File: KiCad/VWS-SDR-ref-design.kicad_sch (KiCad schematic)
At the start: 99 parts, among them J1 RF_IN, J10 IF breakout, J2 IQ_Out, J3 SI5351 board, J4 Conn_01x20_Socket, J5 Conn_01x20_Socket, J6 I2C breakout, J7 Power breakout, J8 GPIO Breakout, J9 GPIO Breakout, U1 GALI-S66, U2 74CBTLV3253DR, U3 MC33078, U4 MC33078, U5 RASPBERRY-PICO

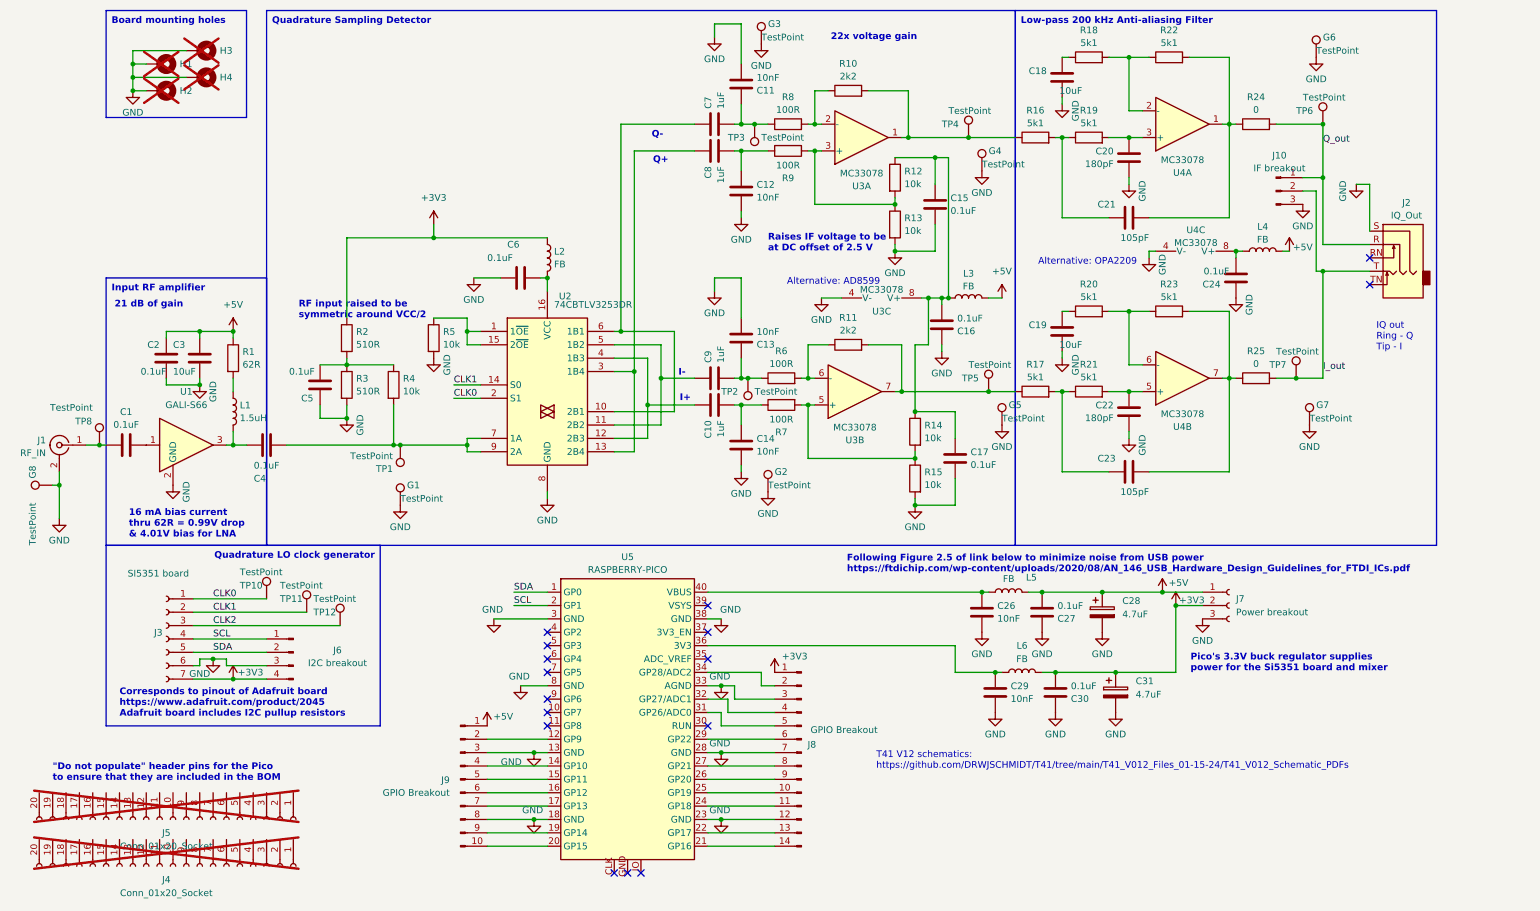
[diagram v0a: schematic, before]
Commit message: Cleaned up the schematic (removed unnecessary components), replaced R/C footprints with 0603, replaced testpoints wit smd footprints, made mounting holes smaller
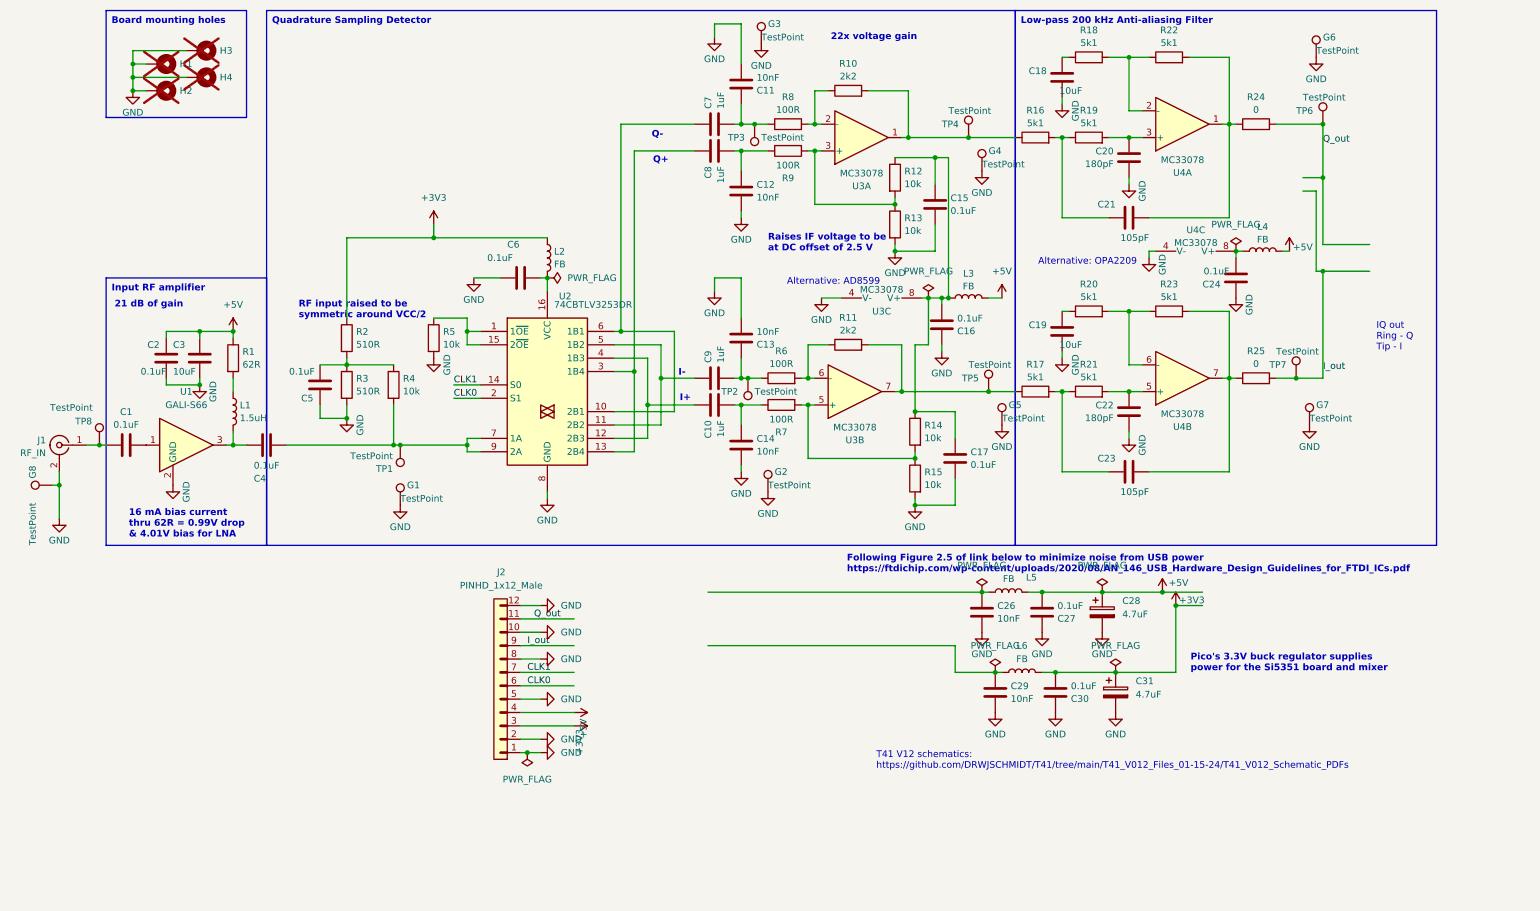
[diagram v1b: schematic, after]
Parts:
- removed J10: IF breakout, symbol Connector:Conn_01x03_Pin
- removed J2: IQ_Out, VWS-SDR:Jack_3.5mm_STX-3081_Horizontal, symbol Connector_Audio:AudioJack3_SwitchTR
- removed J3: SI5351 board, VWS-SDR:Adafruit_Si5351, symbol Connector:Conn_01x07_Socket
- removed J4, J5: Conn_01x20_Socket, symbol Connector:Conn_01x20_Socket
- removed J6: I2C breakout, Connector_PinHeader_2.54mm:PinHeader_1x04_P2.54mm_Vertical, symbol Connector:Conn_01x04_Pin
- removed J7: Power breakout, Connector_PinHeader_2.54mm:PinHeader_1x03_P2.54mm_Vertical, symbol Connector:Conn_01x03_Socket
- removed J8: GPIO Breakout, symbol Connector:Conn_01x14_Pin
- removed J9: GPIO Breakout, symbol Connector:Conn_01x10_Pin
- removed TP10, TP11, TP12: TestPoint, Connector_PinHeader_2.54mm:PinHeader_1x01_P2.54mm_Vertical, symbol Connector:TestPoint
- removed U5: RASPBERRY-PICO, VWS-SDR:Raspberry_pico_pin_or_castellation_footprint, symbol VWS-SDR:RASPBERRY-PICO
- added J2: PINHD_1x12_Male, Connector_PinHeader_2.54mm:PinHeader_1x12_P2.54mm_Vertical, symbol PCM_SL_Pin_Headers:PINHD_1x12_Male
- C1, C10, C11, C12, C13, C14, C15, C16, C17, C18, C19, C2, C20, C21, C22, C23, C24, C26, C27, C29, C3, C30, C4, C5, C6, C7, C8, C9: footprint Capacitor_SMD:C_1206_3216Metric -> Capacitor_SMD:C_0603_1608Metric
- G1, G2, G3, G4, G5, G6, G7, G8, TP1, TP2, TP3, TP4, TP5, TP6, TP7, TP8: footprint Connector_PinHeader_2.54mm:PinHeader_1x01_P2.54mm_Vertical -> TestPoint:TestPoint_Pad_D1.0mm
- H1, H2, H3, H4: footprint MountingHole:MountingHole_4.3mm_M4_DIN965_Pad -> MountingHole:MountingHole_3.2mm_M3_DIN965_Pad
- J1: footprint Connector_Coaxial:SMA_Amphenol_901-144_Vertical -> Connector_Coaxial:SMA_Molex_73251-1153_EdgeMount_Horizontal
- L1, L2, L3, L4, L5, L6, R1, R10, R11, R12, R13, R14, R15, R16, R17, R18, R19, R2, R20, R21, R22, R23, R24, R25, R3, R4, R5, R6, R7, R8, R9: footprint Resistor_SMD:R_1206_3216Metric -> Resistor_SMD:R_0603_1608Metric
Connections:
- net +3V3: now also J2.3
- net +5V: now also J2.4
- net CLK0: now also J2.6
- net CLK1: now also J2.7
- net GND: now also J2.1, J2.10, J2.12, J2.2, J2.5, J2.8
- net I_out: now also J2.9
- net Q_out: now also J2.11
- no-connect marks 16 -> 0
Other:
- note removed: ""Do not populate" header pins for the Pico to ensure that they are included in the BOM"
- note removed: "Corresponds to pinout of Adafruit board https://www.adafruit.com/product/2045 Adafruit board includes I2C pullup resistors"
